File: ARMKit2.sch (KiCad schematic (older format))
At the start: 35 parts, among them P1 CONN_01X06, P2 CONN_01X32, P3 CONN_01X32, P4 USB_B, SW1 SW_PUSH, SW2 SW_PUSH, U1 STM32F405RG, U2 LT1761, Y1 Crystal, Y2 Crystal

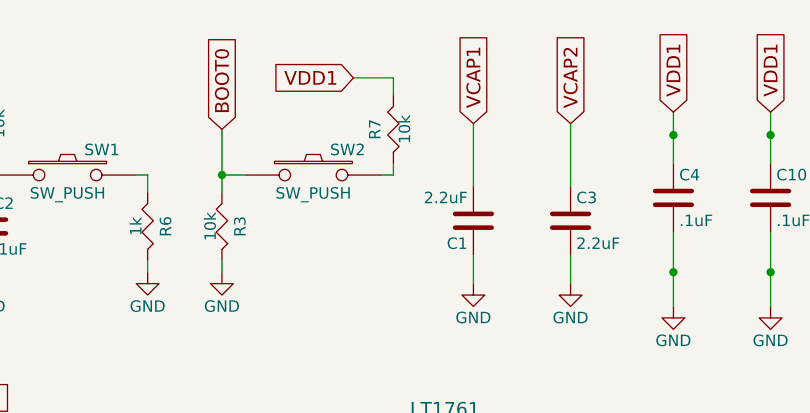
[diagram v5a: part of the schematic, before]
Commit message: Fixed BOOT0 pullup resistor value
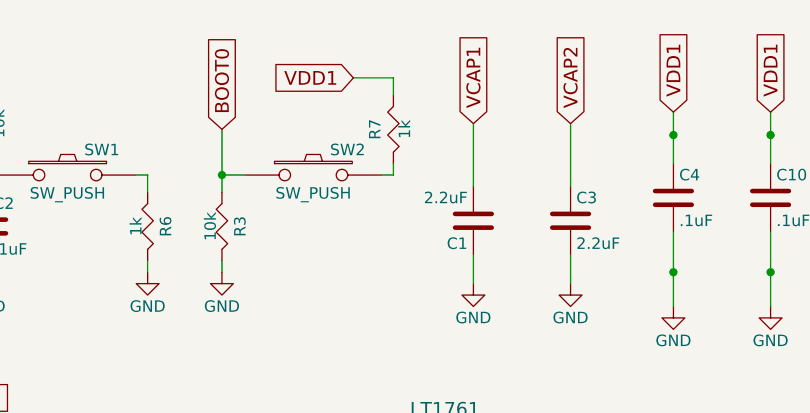
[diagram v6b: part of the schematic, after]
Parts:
- R7: value 10k -> 1k
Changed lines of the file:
@@
 P 7150 925
 F 0 "R7" V 7230 925 50  0000 C CNN
-F 1 "10k" V 7100 925 50  0000 C CNN
+F 1 "1k" V 7100 925 50  0000 C CNN
 F 2 "Capacitors_SMD:C_0805" V 7080 925 30  0001 C CNN
 F 3 "" H 7150 925 30  0000 C CNN

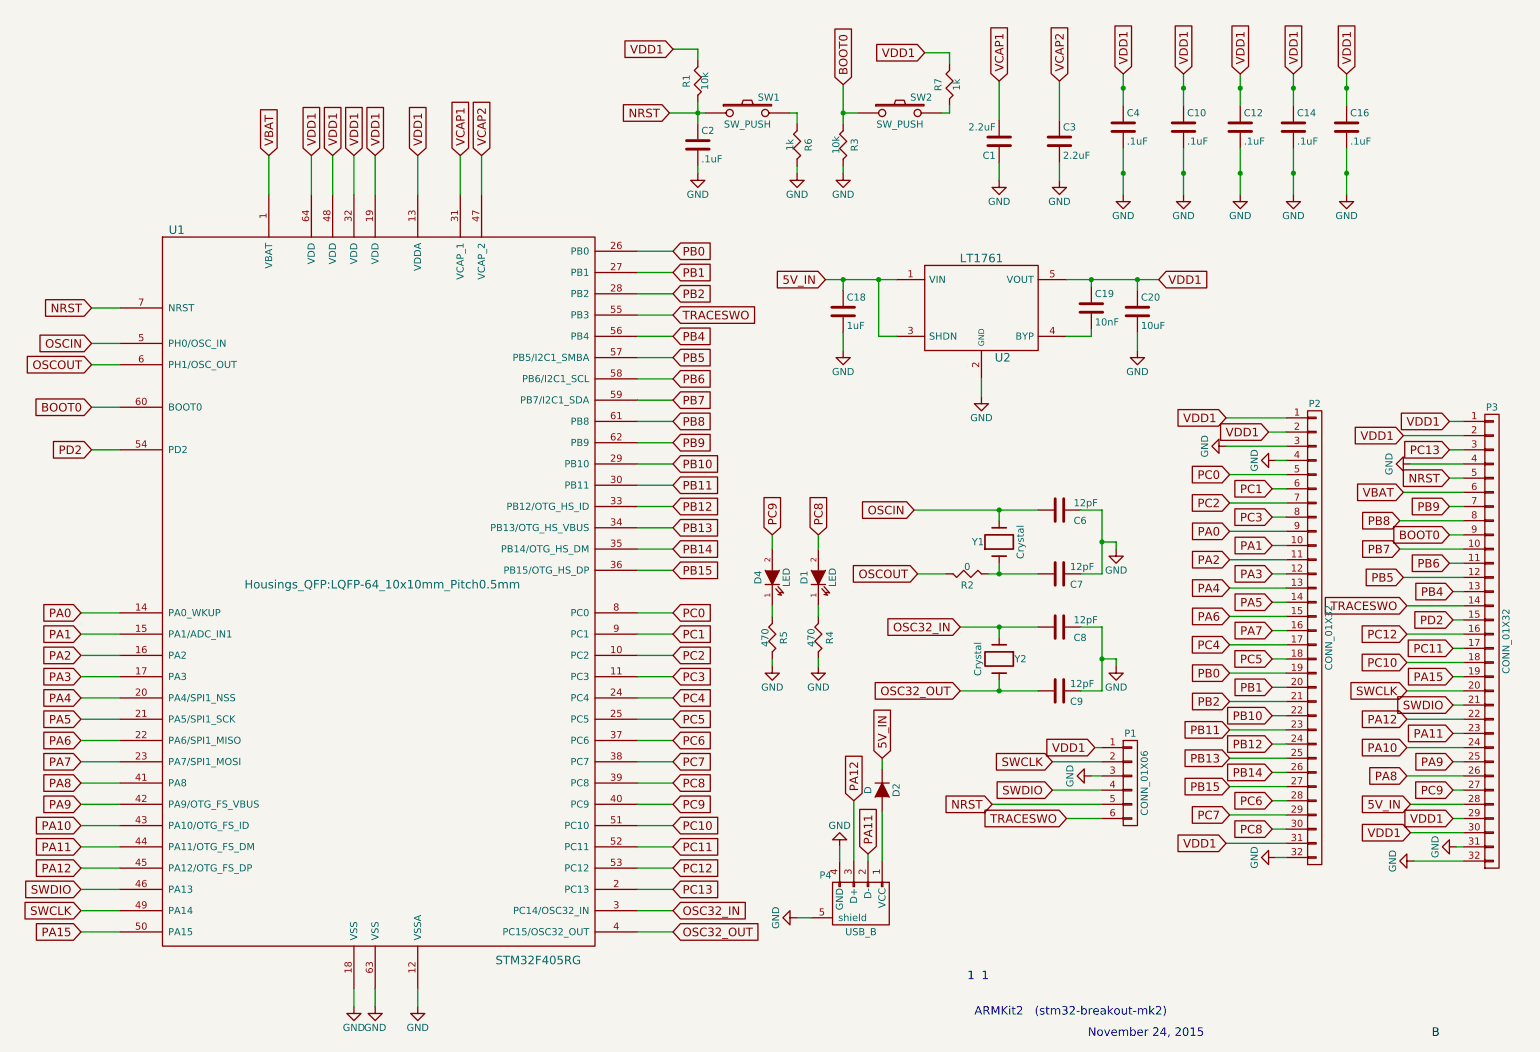
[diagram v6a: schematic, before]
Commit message: Updated for STM32F41x, STM32F4x1 compatibility
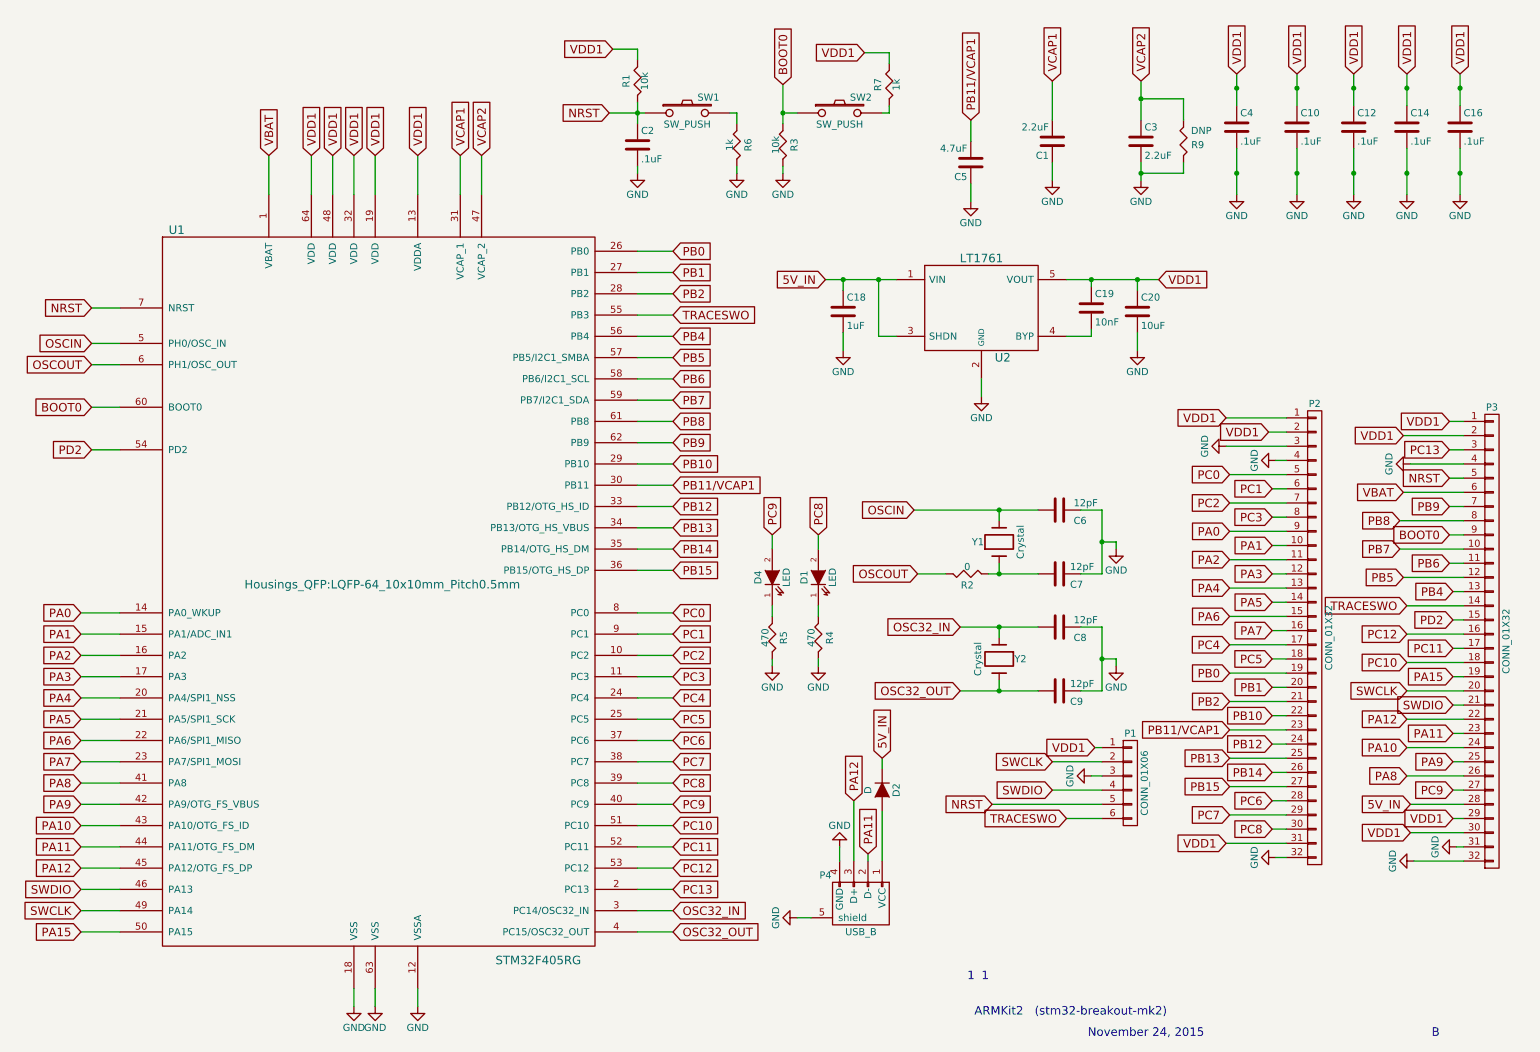
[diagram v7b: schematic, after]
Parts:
- added C5: 4.7uF, Capacitors_SMD:C_0805, symbol C
- added R9: DNP, Capacitors_SMD:C_0805, symbol R
- Y1: footprint Crystals:Crystal_HC49-SD_SMD -> Crystals:Crystal_SMD_5032_2Pads
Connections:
- net GND: now also C5.1, R9.2
- net VCAP2: now also R9.1
- net PB11 renamed PB11/VCAP1
- net PB11/VCAP1: now also C5.2
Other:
- moved on the sheet: C1, C10, C12, C14, C16, C2, C3, C4, R1, R3, R6, R7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

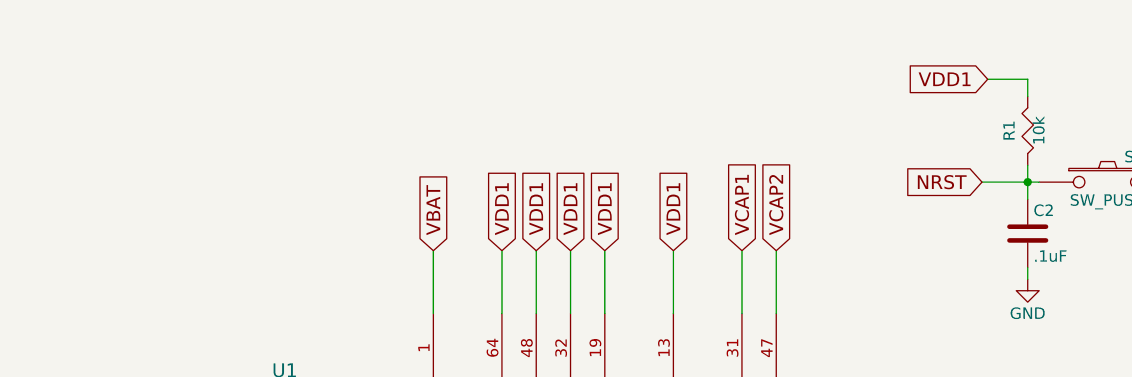
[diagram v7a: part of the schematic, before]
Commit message: Added population notes
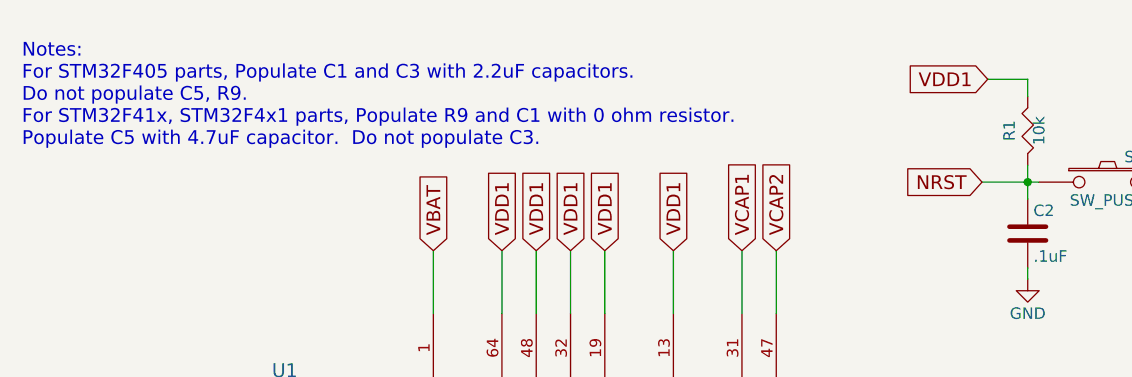
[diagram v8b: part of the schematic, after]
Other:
- note added: "Notes:\nFor STM32F405 parts, Populate C1 and C3 with 2.2uF capacitors. \nDo not populate C5, R9.\nFor STM32F41x, STM32F4x1 parts, Populate R9 and C1 with 0 ohm resistor. \nPopulate C5 with 4.7uF capacitor. Do not populate C3."
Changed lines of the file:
@@
 Wire Wire Line
 	7300 1325 7300 1175
+Text Notes 550  975  0    60   ~ 0
+Notes:\nFor STM32F405 parts, Populate C1 and C3 with 2.2uF capacitors.  \nDo not populate C5, R9.\nFor STM32F41x, STM32F4x1 parts, Populate R9 and C1 with 0 ohm resistor. \nPopulate C5 with 4.7uF capacitor.  Do not populate C3.
 $EndSCHEMATC
